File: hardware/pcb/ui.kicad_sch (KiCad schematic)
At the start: 11 parts, among them J3 Conn_01x06, J4 Conn_01x06, U3 DRV8833PWP

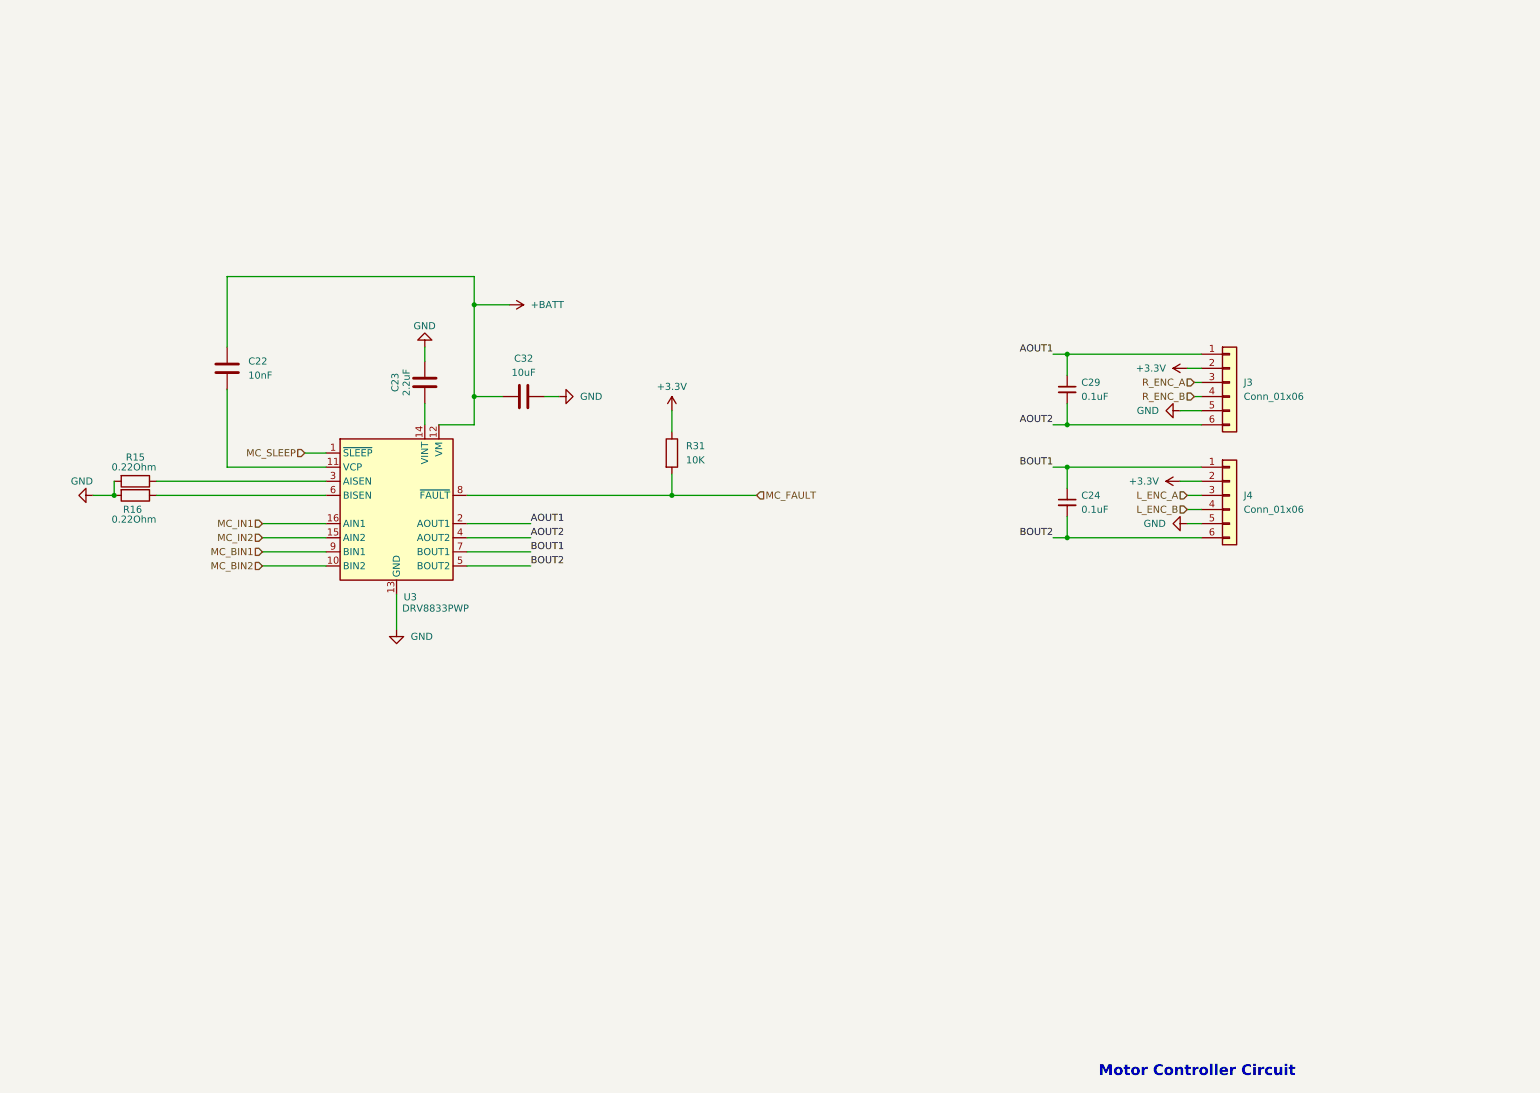
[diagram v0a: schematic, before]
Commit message: hardware: freeze schematic v1 after complete PCB redesign
Complete PCB and schematic refresh with reorganized sheets (psu, ui),
updated MCU/motor/sensor subsystems, and v1 schematic baseline frozen.
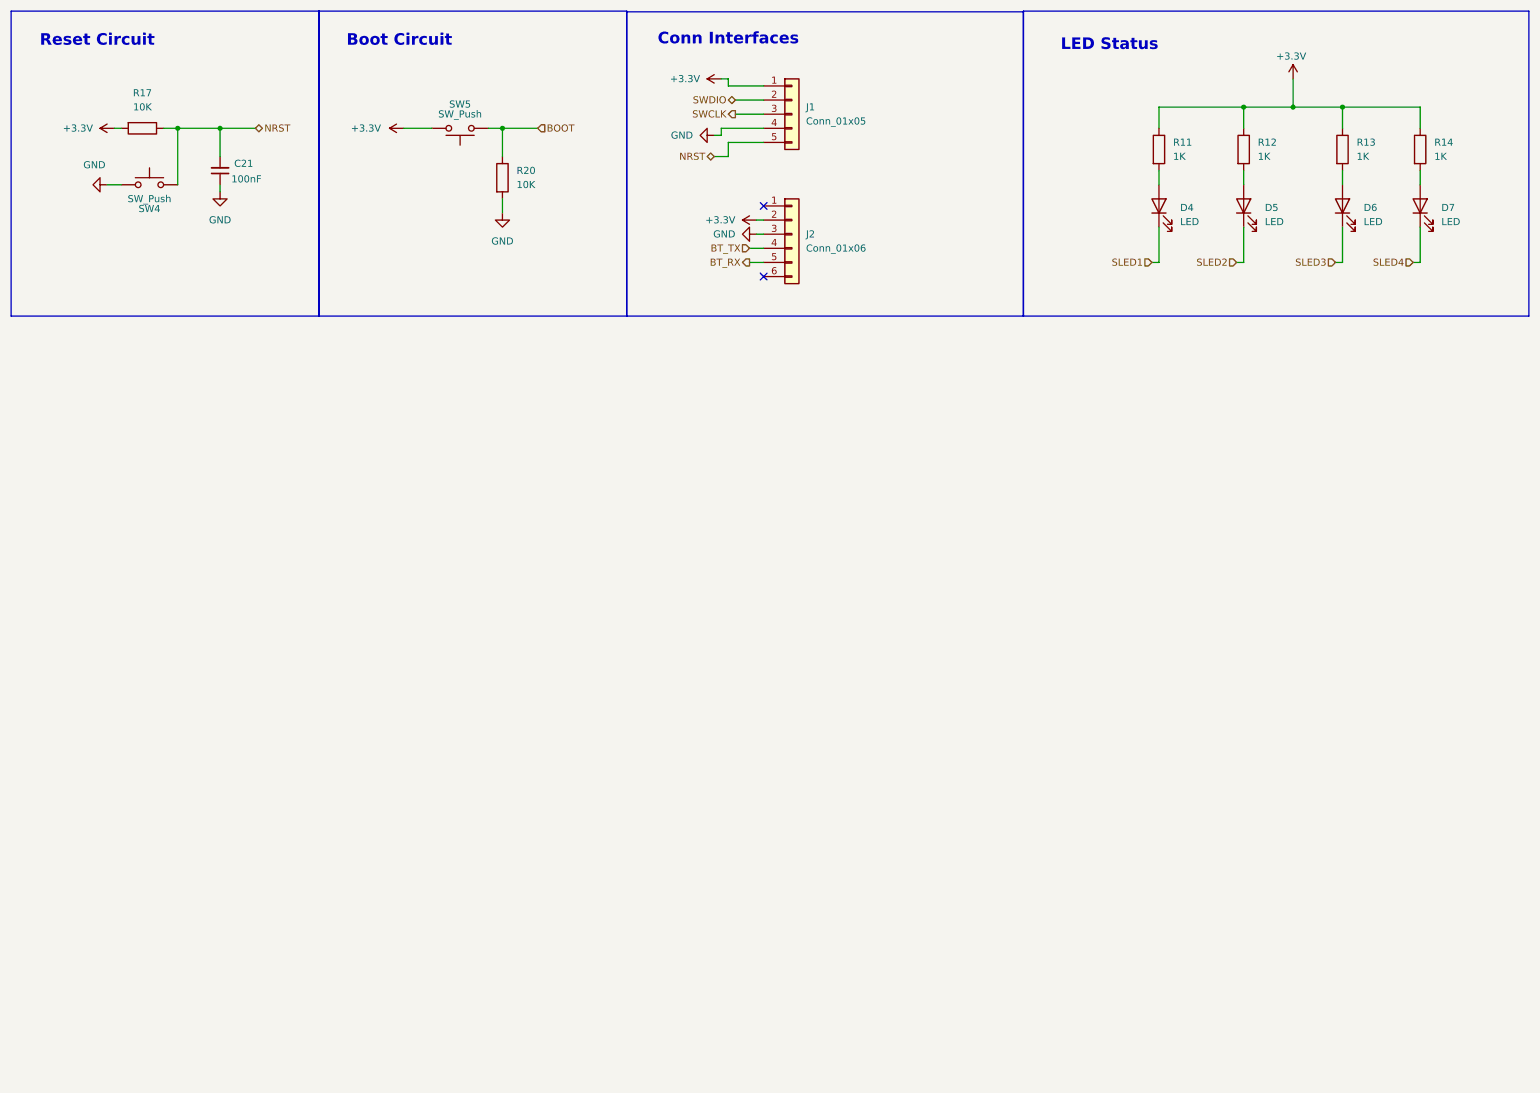
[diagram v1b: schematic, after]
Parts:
- removed C22: 10nF, Capacitor_SMD:C_0603_1608Metric_Pad1.08x0.95mm_HandSolder, symbol Device:C
- removed C23: 2.2uF, Capacitor_SMD:C_0603_1608Metric_Pad1.08x0.95mm_HandSolder, symbol Device:C
- removed C24, C29: 0.1uF, Capacitor_SMD:C_0603_1608Metric_Pad1.08x0.95mm_HandSolder, symbol Device:C_Small
- removed C32: 10uF, Capacitor_SMD:C_0603_1608Metric_Pad1.08x0.95mm_HandSolder, symbol Device:C
- removed J3, J4: Conn_01x06, Connector_PinHeader_2.54mm:PinHeader_1x06_P2.54mm_Vertical, symbol Connector_Generic:Conn_01x06
- removed R15, R16: 0.22Ohm, Resistor_SMD:R_1206_3216Metric_Pad1.30x1.75mm_HandSolder, symbol Device:R
- removed R31: 10K, Resistor_SMD:R_0805_2012Metric_Pad1.20x1.40mm_HandSolder, symbol Device:R
- removed U3: DRV8833PWP, Package_SO:HTSSOP-16-1EP_4.4x5mm_P0.65mm_EP3.4x5mm_Mask2.46x2.31mm_ThermalVias, symbol Driver_Motor:DRV8833PWP
- added C21: 100nF, Capacitor_SMD:C_0805_2012Metric_Pad1.18x1.45mm_HandSolder, symbol Device:C_Small
- added D4, D5, D6, D7: LED, LED_SMD:LED_0805_2012Metric_Pad1.15x1.40mm_HandSolder, symbol Device:LED
- added J1: Conn_01x05, Connector_PinHeader_1.00mm:PinHeader_1x05_P1.00mm_Vertical, symbol Connector_Generic:Conn_01x05
- added J2: Conn_01x06, Connector_PinHeader_1.00mm:PinHeader_1x06_P1.00mm_Vertical, symbol Connector_Generic:Conn_01x06
- added R11, R12, R13, R14: 1K, Resistor_SMD:R_0805_2012Metric_Pad1.20x1.40mm_HandSolder, symbol Device:R
- added R17, R20: 10K, Resistor_SMD:R_0805_2012Metric_Pad1.20x1.40mm_HandSolder, symbol Device:R
- added SW4, SW5: SW_Push, Button_Switch_SMD:SW_SPST_B3U-3000P, symbol Switch:SW_Push
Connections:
- net +3.3V: now also J1.1 (Pin_1), J2.2 (Pin_2), R11.1, R12.1, R13.1, R14.1, R17.2, SW5.2
- net GND: now also C21.1, J1.4 (Pin_4), J2.3 (Pin_3), R20.2, SW4.1
- new net: D7.2 (A), R14.2
- new net: D4.2 (A), R11.2
- new net: D6.2 (A), R13.2
- new net: D5.2 (A), R12.2
- new net BOOT: R20.1, SW5.1
- new net BT_RX: J2.5 (Pin_5)
- new net BT_TX: J2.4 (Pin_4)
- new net NRST: C21.2, J1.5 (Pin_5), R17.1, SW4.2
- new net SLED1: D4.1 (K)
- new net SLED2: D5.1 (K)
- new net SLED3: D6.1 (K)
- new net SLED4: D7.1 (K)
- new net SWCLK: J1.3 (Pin_3)
- new net SWDIO: J1.2 (Pin_2)
- no-connect marks 0 -> 2
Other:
- note added: "Boot Circuit"
- note added: "Conn Interfaces"
- note added: "LED Status"
- note added: "Reset Circuit"
- note removed: "Motor Controller Circuit"

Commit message: format öncesi commit
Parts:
- C21: footprint Capacitor_SMD:C_0805_2012Metric_Pad1.18x1.45mm_HandSolder -> Capacitor_SMD:C_0603_1608Metric
- D4, D5, D6, D7: footprint LED_SMD:LED_0805_2012Metric_Pad1.15x1.40mm_HandSolder -> LED_SMD:LED_0603_1608Metric
- R11, R12, R13, R14, R17, R20: footprint Resistor_SMD:R_0805_2012Metric_Pad1.20x1.40mm_HandSolder -> Resistor_SMD:R_0603_1608Metric
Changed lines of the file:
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@@
 			)
 		)
-		(property "Footprint" "Resistor_SMD:R_0805_2012Metric_Pad1.20x1.40mm_HandSolder"
+		(property "Footprint" "Resistor_SMD:R_0603_1608Metric"
 			(at 263.652 36.83 90)
 			(hide yes)
@@
 			)
 		)
-		(property "Footprint" "LED_SMD:LED_0805_2012Metric_Pad1.15x1.40mm_HandSolder"
+		(property "Footprint" "LED_SMD:LED_0603_1608Metric"
 			(at 218.44 46.99 0)
 			(hide yes)
@@
 			)
 		)
-		(property "Footprint" "Resistor_SMD:R_0805_2012Metric_Pad1.20x1.40mm_HandSolder"
+		(property "Footprint" "Resistor_SMD:R_0603_1608Metric"
 			(at 249.682 36.83 90)
 			(hide yes)
@@
 			)
 		)
-		(property "Footprint" "LED_SMD:LED_0805_2012Metric_Pad1.15x1.40mm_HandSolder"
+		(property "Footprint" "LED_SMD:LED_0603_1608Metric"
 			(at 233.68 46.99 0)
 			(hide yes)
@@
 			)
 		)
-		(property "Footprint" "Capacitor_SMD:C_0805_2012Metric_Pad1.18x1.45mm_HandSolder"
+		(property "Footprint" "Capacitor_SMD:C_0603_1608Metric"
 			(at 49.53 40.64 0)
 			(hide yes)
@@
 			)
 		)
-		(property "Footprint" "Resistor_SMD:R_0805_2012Metric_Pad1.20x1.40mm_HandSolder"
+		(property "Footprint" "Resistor_SMD:R_0603_1608Metric"
 			(at 35.56 31.242 90)
 			(hide yes)
@@
 			)
 		)
-		(property "Footprint" "Resistor_SMD:R_0805_2012Metric_Pad1.20x1.40mm_HandSolder"
+		(property "Footprint" "Resistor_SMD:R_0603_1608Metric"
 			(at 98.552 41.91 90)
 			(hide yes)
@@
 			)
 		)
-		(property "Footprint" "LED_SMD:LED_0805_2012Metric_Pad1.15x1.40mm_HandSolder"
+		(property "Footprint" "LED_SMD:LED_0603_1608Metric"
 			(at 251.46 46.99 0)
 			(hide yes)
@@
 			)
 		)
-		(property "Footprint" "Resistor_SMD:R_0805_2012Metric_Pad1.20x1.40mm_HandSolder"
+		(property "Footprint" "Resistor_SMD:R_0603_1608Metric"
 			(at 231.902 36.83 90)
 			(hide yes)
@@
 			)
 		)
-		(property "Footprint" "LED_SMD:LED_0805_2012Metric_Pad1.15x1.40mm_HandSolder"
+		(property "Footprint" "LED_SMD:LED_0603_1608Metric"
 			(at 265.43 46.99 0)
 			(hide yes)
@@
 			)
 		)
-		(property "Footprint" "Resistor_SMD:R_0805_2012Metric_Pad1.20x1.40mm_HandSolder"
+		(property "Footprint" "Resistor_SMD:R_0603_1608Metric"
 			(at 216.662 36.83 90)
 			(hide yes)
